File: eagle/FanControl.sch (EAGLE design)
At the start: 18 parts, among them U1 LP2985

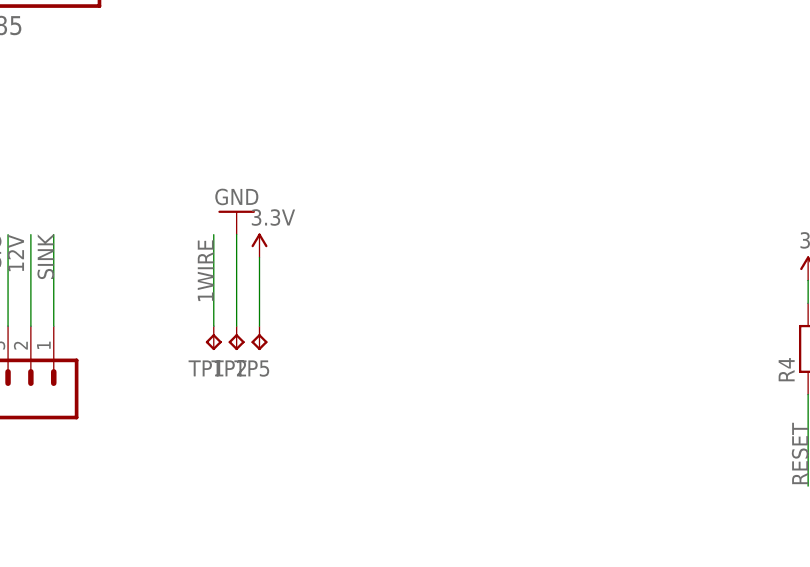
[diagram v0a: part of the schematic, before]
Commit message: Added extra pads for another 1-Wire device on the bottom layer.
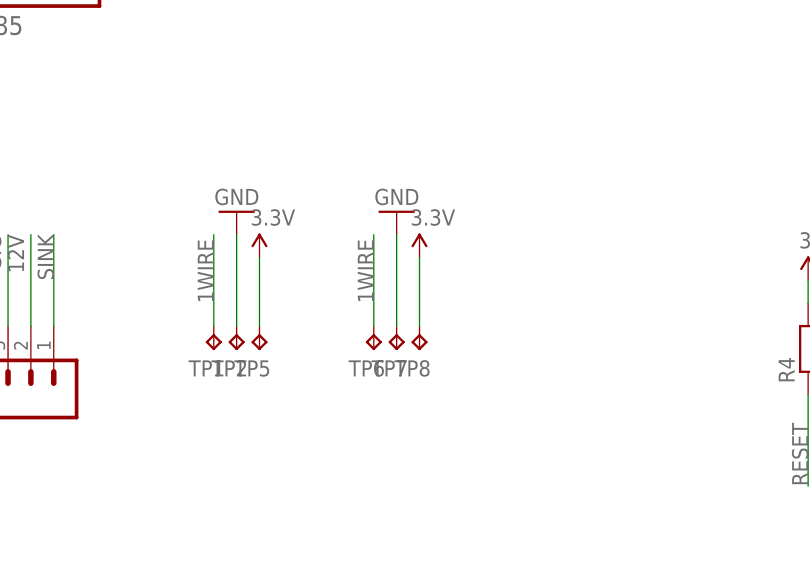
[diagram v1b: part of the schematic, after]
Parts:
- added TP6, TP7, TP8: TPB1,27, testpad:TPB1,27
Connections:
- net 1WIRE: now also TP6.TP
- net 3.3V: now also TP8.TP
- net GND: now also TP7.TP
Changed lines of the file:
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@@
 <grid distance="0.1" unitdist="inch" unit="inch" style="lines" multiple="1" display="no" altdistance="0.01" altunitdist="inch" altunit="inch"/>
 <layers>
-<layer number="1" name="Top" color="4" fill="1" visible="no" active="no"/>
-<layer number="16" name="Bottom" color="1" fill="1" visible="no" active="no"/>
-<layer number="17" name="Pads" color="2" fill="1" visible="no" active="no"/>
-<layer number="18" name="Vias" color="2" fill="1" visible="no" active="no"/>
-<layer number="19" name="Unrouted" color="6" fill="1" visible="no" active="no"/>
-<layer number="20" name="Dimension" color="15" fill="1" visible="no" active="no"/>
-<layer number="21" name="tPlace" color="7" fill="1" visible="no" active="no"/>
-<layer number="22" name="bPlace" color="7" fill="1" visible="no" active="no"/>
-<layer number="23" name="tOrigins" color="15" fill="1" visible="no" active="no"/>
-<layer number="24" name="bOrigins" color="15" fill="1" visible="no" active="no"/>
-<layer number="25" name="tNames" color="7" fill="1" visible="no" active="no"/>
-<layer number="26" name="bNames" color="7" fill="1" visible="no" active="no"/>
-<layer number="27" name="tValues" color="7" fill="1" visible="no" active="no"/>
-<layer number="28" name="bValues" color="7" fill="1" visible="no" active="no"/>
+<layer number="1" name="Top" color="4" fill="1" visible="yes" active="no"/>
+<layer number="16" name="Bottom" color="1" fill="1" visible="yes" active="no"/>
+<layer number="17" name="Pads" color="2" fill="1" visible="yes" active="no"/>
+<layer number="18" name="Vias" color="2" fill="1" visible="yes" active="no"/>
+<layer number="19" name="Unrouted" color="6" fill="1" visible="yes" active="no"/>
+<layer number="20" name="Dimension" color="15" fill="1" visible="yes" active="no"/>
+<layer number="21" name="tPlace" color="7" fill="1" visible="yes" active="no"/>
+<layer number="22" name="bPlace" color="7" fill="1" visible="yes" active="no"/>
+<layer number="23" name="tOrigins" color="15" fill="1" visible="yes" active="no"/>
+<layer number="24" name="bOrigins" color="15" fill="1" visible="yes" active="no"/>
+<layer number="25" name="tNames" color="7" fill="1" visible="yes" active="no"/>
+<layer number="26" name="bNames" color="7" fill="1" visible="yes" active="no"/>
+<layer number="27" name="tValues" color="7" fill="1" visible="yes" active="no"/>
+<layer number="28" name="bValues" color="7" fill="1" visible="yes" active="no"/>
 <layer number="29" name="tStop" color="7" fill="3" visible="no" active="no"/>
 <layer number="30" name="bStop" color="7" fill="6" visible="no" active="no"/>
@@
 <layer number="35" name="tGlue" color="7" fill="4" visible="no" active="no"/>
 <layer number="36" name="bGlue" color="7" fill="5" visible="no" active="no"/>
-<layer number="37" name="tTest" color="7" fill="1" visible="no" active="no"/>
-<layer number="38" name="bTest" color="7" fill="1" visible="no" active="no"/>
+<layer number="37" name="tTest" color="7" fill="1" visible="yes" active="no"/>
+<layer number="38" name="bTest" color="7" fill="1" visible="yes" active="no"/>
 <layer number="39" name="tKeepout" color="4" fill="11" visible="no" active="no"/>
 <layer number="40" name="bKeepout" color="1" fill="11" visible="no" active="no"/>
@@
 <layer number="44" name="Drills" color="7" fill="1" visible="no" active="no"/>
 <layer number="45" name="Holes" color="7" fill="1" visible="no" active="no"/>
-<layer number="46" name="Milling" color="3" fill="1" visible="no" active="no"/>
-<layer number="47" name="Measures" color="7" fill="1" visible="no" active="no"/>
-<layer number="48" name="Document" color="7" fill="1" visible="no" active="no"/>
-<layer number="49" name="Reference" color="7" fill="1" visible="no" active="no"/>
-<layer number="50" name="dxf" color="7" fill="1" visible="no" active="no"/>
-<layer number="51" name="tDocu" color="7" fill="1" visible="no" active="no"/>
-<layer number="52" name="bDocu" color="7" fill="1" visible="no" active="no"/>
-<layer number="53" name="tGND_GNDA" color="7" fill="9" visible="no" active="no"/>
-<layer number="54" name="bGND_GNDA" color="1" fill="9" visible="no" active="no"/>
-<layer number="56" name="wert" color="7" fill="1" visible="no" active="no"/>
-<layer number="57" name="tCAD" color="7" fill="1" visible="no" active="no"/>
+<layer number="46" name="Milling" color="3" fill="1" visible="yes" active="no"/>
+<layer number="47" name="Measures" color="7" fill="1" visible="yes" active="no"/>
+<layer number="48" name="Document" color="7" fill="1" visible="yes" active="no"/>
+<layer number="49" name="Reference" color="7" fill="1" visible="yes" active="no"/>
+<layer number="50" name="dxf" color="7" fill="1" visible="yes" active="no"/>
+<layer number="51" name="tDocu" color="7" fill="1" visible="yes" active="no"/>
+<layer number="52" name="bDocu" color="7" fill="1" visible="yes" active="no"/>
+<layer number="53" name="tGND_GNDA" color="7" fill="9" visible="yes" active="no"/>
+<layer number="54" name="bGND_GNDA" color="1" fill="9" visible="yes" active="no"/>
+<layer number="56" name="wert" color="7" fill="1" visible="yes" active="no"/>
+<layer number="57" name="tCAD" color="7" fill="1" visible="yes" active="no"/>
 <layer number="90" name="Modules" color="5" fill="1" visible="yes" active="yes"/>
 <layer number="91" name="Nets" color="2" fill="1" visible="yes" active="yes"/>
@@
 <part name="TP5" library="testpad" deviceset="TP" device="B1,27"/>
 <part name="SUPPLY5" library="SparkFun-Aesthetics" deviceset="3.3V" device=""/>
+<part name="GND6" library="SparkFun-Aesthetics" deviceset="GND" device=""/>
+<part name="TP6" library="testpad" deviceset="TP" device="B1,27"/>
+<part name="TP7" library="testpad" deviceset="TP" device="B1,27"/>
+<part name="TP8" library="testpad" deviceset="TP" device="B1,27"/>
+<part name="SUPPLY8" library="SparkFun-Aesthetics" deviceset="3.3V" device=""/>
 </parts>
 <sheets>
@@
 <instance part="TP5" gate="G$1" x="66.04" y="10.16" rot="R180"/>
 <instance part="SUPPLY5" gate="G$1" x="66.04" y="20.32"/>
+<instance part="GND6" gate="1" x="81.28" y="25.4" rot="R180"/>
+<instance part="TP6" gate="G$1" x="78.74" y="10.16" rot="R180"/>
+<instance part="TP7" gate="G$1" x="81.28" y="10.16" rot="R180"/>
+<instance part="TP8" gate="G$1" x="83.82" y="10.16" rot="R180"/>
+<instance part="SUPPLY8" gate="G$1" x="83.82" y="20.32"/>
 </instances>
 <busses>
@@
 <pinref part="TP2" gate="G$1" pin="TP"/>
 </segment>
+<segment>
+<wire x1="81.28" y1="12.7" x2="81.28" y2="22.86" width="0.1524" layer="91"/>
+<pinref part="GND6" gate="1" pin="GND"/>
+<pinref part="TP7" gate="G$1" pin="TP"/>
+</segment>
 </net>
 <net name="12V" class="0">
@@
 <wire x1="66.04" y1="20.32" x2="66.04" y2="12.7" width="0.1524" layer="91"/>
 </segment>
+<segment>
+<pinref part="SUPPLY8" gate="G$1" pin="3.3V"/>
+<pinref part="TP8" gate="G$1" pin="TP"/>
+<wire x1="83.82" y1="20.32" x2="83.82" y2="12.7" width="0.1524" layer="91"/>
+</segment>
 </net>
 <net name="SIG" class="0">
@@
 <label x="111.76" y="88.9" size="1.778" layer="95"/>
 </segment>
-</net>
+<segment>
+<wire x1="78.74" y1="12.7" x2="78.74" y2="22.86" width="0.1524" layer="91"/>
+<label x="78.74" y="15.24" size="1.778" layer="95" rot="R90"/>
+<pinref part="TP6" gate="G$1" pin="TP"/>
+</segment>
+</net>
